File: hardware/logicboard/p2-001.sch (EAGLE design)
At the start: 59 parts, among them IC1 74LS07N, IC11 74LS153D, IC12 LTC485S, IC13 LTC485S, IC2 4066N, J1 MKR, J11 Qwiic, J12 Qwiic, J13 Qwiic, J14 Qwiic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

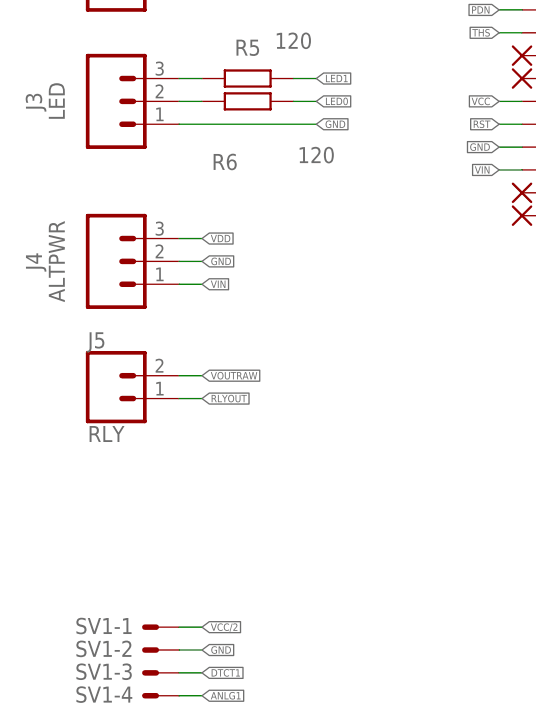
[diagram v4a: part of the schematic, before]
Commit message: Changed Relay port and Alt. Power port.
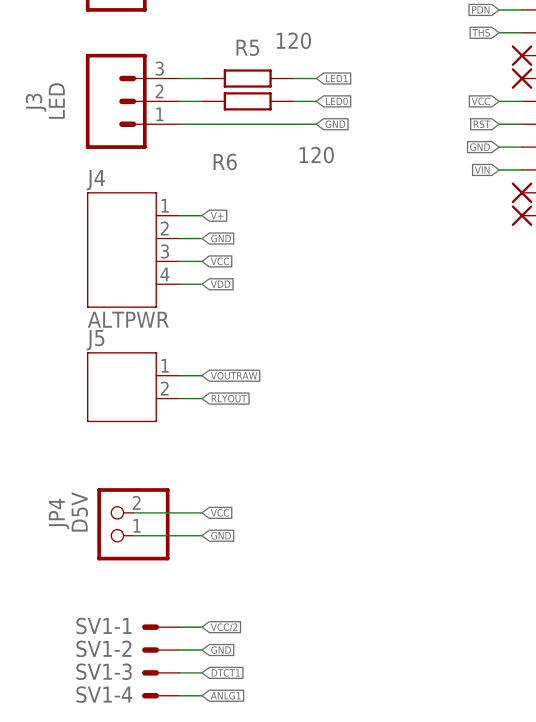
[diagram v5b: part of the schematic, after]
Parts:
- added JP4: D5V, pinhead:PINHD-1X2
- J4: device SparkFun-Connectors:CONN_03JST-PTH-VERT -> jst-ph:JST-PH4
- J5: value RLY -> (none); device SparkFun-Connectors:CONN_02JST-PTH-2 -> jst-ph:JST-PH2
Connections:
- net GND: now also JP4.1
- net RLYOUT: now also J5.2; no longer J5.1
- net V+: now also J4.1
- net VCC: now also J4.3, JP4.2
- net VDD: now also J4.4; no longer J4.3
- net VIN: no longer J4.1
- net VOUTRAW: now also J5.1; no longer J5.2
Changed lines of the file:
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@@
 <part name="SUPPLY54" library="supply2" deviceset="GND" device=""/>
 <part name="JP1" library="pinhead" library_urn="urn:adsk.eagle:library:325" deviceset="PINHD-1X2" device="" package3d_urn="urn:adsk.eagle:package:22435/2" value="MPXJMP"/>
-<part name="J4" library="SparkFun-Connectors" deviceset="CONN_03" device="JST-PTH-VERT" value="ALTPWR"/>
 <part name="D1" library="SparkFun-DiscreteSemi" library_urn="urn:adsk.eagle:library:514" deviceset="DIODE" device="-1N4148" package3d_urn="urn:adsk.eagle:package:38452/1" value=""/>
 <part name="J2" library="SparkFun-Connectors" deviceset="CONN_03" device="JST-PTH-VERT" value="GPIO"/>
@@
 <part name="SUPPLY5" library="supply2" library_urn="urn:adsk.eagle:library:372" deviceset="VCC" device=""/>
 <part name="X14" library="wirepad" library_urn="urn:adsk.eagle:library:412" deviceset="PAD-N" device=""/>
-<part name="J5" library="SparkFun-Connectors" library_urn="urn:adsk.eagle:library:513" deviceset="CONN_02" device="JST-PTH-2" package3d_urn="urn:adsk.eagle:package:38053/1" value="RLY"/>
 <part name="JP3" library="pinhead" library_urn="urn:adsk.eagle:library:325" deviceset="PINHD-2X3" device="" package3d_urn="urn:adsk.eagle:package:22462/2" value="PWRSEL"/>
+<part name="J5" library="jst-ph" deviceset="JST-PH2" device=""/>
+<part name="JP4" library="pinhead" library_urn="urn:adsk.eagle:library:325" deviceset="PINHD-1X2" device="" package3d_urn="urn:adsk.eagle:package:22435/2" value="D5V"/>
+<part name="J4" library="jst-ph" deviceset="JST-PH4" device="" value="ALTPWR"/>
 </parts>
 <sheets>
@@
 <attribute name="VALUE" x="254" y="243.84" size="1.778" layer="96" align="bottom-center"/>
 </instance>
-<instance part="J4" gate="J$1" x="17.78" y="195.58" smashed="yes">
-<attribute name="VALUE" x="12.7" y="195.58" size="1.778" layer="96" rot="R90" align="bottom-center"/>
-<attribute name="NAME" x="10.16" y="195.58" size="1.778" layer="95" rot="R90" align="bottom-center"/>
-</instance>
 <instance part="D1" gate="G$1" x="106.68" y="109.22" smashed="yes" rot="R180">
 <attribute name="NAME" x="106.68" y="114.3" size="1.778" layer="95" align="bottom-center"/>
@@
 </instance>
 <instance part="X14" gate="G$1" x="25.4" y="91.44" smashed="yes"/>
-<instance part="J5" gate="G$1" x="17.78" y="180.34" smashed="yes">
-<attribute name="VALUE" x="15.24" y="175.514" size="1.778" layer="96" font="vector"/>
-<attribute name="NAME" x="15.24" y="185.928" size="1.778" layer="95" font="vector"/>
-</instance>
 <instance part="JP3" gate="A" x="124.46" y="157.48" smashed="yes" rot="R90">
 <attribute name="NAME" x="118.745" y="151.13" size="1.778" layer="95" rot="R90"/>
 <attribute name="VALUE" x="132.08" y="151.13" size="1.778" layer="96" rot="R90"/>
+</instance>
+<instance part="J5" gate="G$1" x="17.78" y="182.88" smashed="yes">
+<attribute name="NAME" x="15.24" y="186.182" size="1.778" layer="95"/>
+<attribute name="VALUE" x="15.24" y="175.514" size="1.778" layer="96"/>
+</instance>
+<instance part="JP4" gate="G$1" x="17.78" y="167.64" smashed="yes" rot="R180">
+<attribute name="NAME" x="12.7" y="167.64" size="1.778" layer="95" rot="R90" align="bottom-center"/>
+<attribute name="VALUE" x="15.24" y="167.64" size="1.778" layer="96" rot="R90" align="bottom-center"/>
+</instance>
+<instance part="J4" gate="A" x="17.78" y="198.12" smashed="yes">
+<attribute name="NAME" x="15.24" y="203.962" size="1.778" layer="95"/>
+<attribute name="VALUE" x="15.24" y="188.214" size="1.778" layer="96"/>
 </instance>
 </instances>
@@
 </segment>
 <segment>
-<pinref part="J4" gate="J$1" pin="2"/>
-<wire x1="25.4" y1="195.58" x2="27.94" y2="195.58" width="0.1524" layer="91"/>
-<label x="27.94" y="195.58" size="0.8128" layer="95" xref="yes"/>
+<pinref part="JP4" gate="G$1" pin="1"/>
+<wire x1="20.32" y1="165.1" x2="27.94" y2="165.1" width="0.1524" layer="91"/>
+<label x="27.94" y="165.1" size="0.8128" layer="95" xref="yes"/>
+</segment>
+<segment>
+<pinref part="J4" gate="A" pin="2"/>
+<wire x1="25.4" y1="198.12" x2="27.94" y2="198.12" width="0.1524" layer="91"/>
+<label x="27.94" y="198.12" size="0.8128" layer="95" xref="yes"/>
 </segment>
 </net>
@@
 <wire x1="124.46" y1="154.94" x2="124.46" y2="147.32" width="0.1524" layer="91"/>
 <label x="124.46" y="147.32" size="0.8128" layer="95" rot="R270" xref="yes"/>
+</segment>
+<segment>
+<pinref part="JP4" gate="G$1" pin="2"/>
+<wire x1="20.32" y1="167.64" x2="27.94" y2="167.64" width="0.1524" layer="91"/>
+<label x="27.94" y="167.64" size="0.8128" layer="95" xref="yes"/>
+</segment>
+<segment>
+<pinref part="J4" gate="A" pin="3"/>
+<wire x1="25.4" y1="195.58" x2="27.94" y2="195.58" width="0.1524" layer="91"/>
+<label x="27.94" y="195.58" size="0.8128" layer="95" xref="yes"/>
 </segment>
 </net>
@@
 </segment>
 <segment>
-<pinref part="J4" gate="J$1" pin="3"/>
-<wire x1="25.4" y1="198.12" x2="27.94" y2="198.12" width="0.1524" layer="91"/>
-<label x="27.94" y="198.12" size="0.8128" layer="95" xref="yes"/>
+<pinref part="J4" gate="A" pin="4"/>
+<wire x1="25.4" y1="193.04" x2="27.94" y2="193.04" width="0.1524" layer="91"/>
+<label x="27.94" y="193.04" size="0.8128" layer="95" xref="yes"/>
 </segment>
 </net>
@@
 </net>
 <net name="VIN" class="2">
-<segment>
-<pinref part="J4" gate="J$1" pin="1"/>
-<wire x1="25.4" y1="193.04" x2="27.94" y2="193.04" width="0.1524" layer="91"/>
-<label x="27.94" y="193.04" size="0.8128" layer="95" xref="yes"/>
-</segment>
 <segment>
 <pinref part="MC1" gate="G$1" pin="9V"/>
@@
 </segment>
 <segment>
-<pinref part="J5" gate="G$1" pin="2"/>
 <wire x1="25.4" y1="182.88" x2="27.94" y2="182.88" width="0.1524" layer="91"/>
 <label x="27.94" y="182.88" size="0.8128" layer="95" xref="yes"/>
+<pinref part="J5" gate="G$1" pin="1"/>
 </segment>
 </net>
@@
 </segment>
 <segment>
-<pinref part="J5" gate="G$1" pin="1"/>
 <wire x1="25.4" y1="180.34" x2="27.94" y2="180.34" width="0.1524" layer="91"/>
 <label x="27.94" y="180.34" size="0.8128" layer="95" xref="yes"/>
+<pinref part="J5" gate="G$1" pin="2"/>
 </segment>
 </net>
@@
 <label x="121.92" y="147.32" size="0.8128" layer="95" rot="R270" xref="yes"/>
 </segment>
-</net>
+<segment>
+<pinref part="J4" gate="A" pin="1"/>
+<wire x1="25.4" y1="200.66" x2="27.94" y2="200.66" width="0.1524" layer="91"/>
+<label x="27.94" y="200.66" size="0.8128" layer="95" xref="yes"/>
+</segment>
+</net>

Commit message: List of components.
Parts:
- removed R6: 120, resistor:R-EU_0204/5
- added R4: 120, resistor:R-EU_0204/5
- renumbered J6 to JP5
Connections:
- net LED0: now also R5.2; no longer R6.2
- net LED0A: now also R5.1; no longer R6.1
- net LED1: now also R4.2; no longer R5.2
- net LED1A: now also R4.1; no longer R5.1
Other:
- moved on the sheet: R5
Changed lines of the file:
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@@
 <part name="SUPPLY29" library="supply2" deviceset="GND" device=""/>
 <part name="J1" library="SparkFun-Connectors" library_urn="urn:adsk.eagle:library:513" deviceset="CONN_05" device="JST" package3d_urn="urn:adsk.eagle:package:38120/1" value="MKR"/>
-<part name="R5" library="resistor" library_urn="urn:adsk.eagle:library:348" deviceset="R-EU_" device="0204/5" package3d_urn="urn:adsk.eagle:package:23488/1" value="120"/>
+<part name="R4" library="resistor" library_urn="urn:adsk.eagle:library:348" deviceset="R-EU_" device="0204/5" package3d_urn="urn:adsk.eagle:package:23488/1" value="120"/>
 <part name="SUPPLY12" library="supply2" deviceset="GND" device=""/>
 <part name="JP0" library="pinhead" library_urn="urn:adsk.eagle:library:325" deviceset="PINHD-1X1" device="" package3d_urn="urn:adsk.eagle:package:22485/2" value="GNDPIN"/>
@@
 <part name="H1" library="SparkFun-Hardware" library_urn="urn:adsk.eagle:library:519" deviceset="STAND-OFF" device="" package3d_urn="urn:adsk.eagle:package:38630/1"/>
 <part name="H2" library="SparkFun-Hardware" library_urn="urn:adsk.eagle:library:519" deviceset="STAND-OFF" device="" package3d_urn="urn:adsk.eagle:package:38630/1"/>
-<part name="J6" library="SparkFun-Connectors" library_urn="urn:adsk.eagle:library:513" deviceset="CONN_05" device="" package3d_urn="urn:adsk.eagle:package:38104/1" value="RTC"/>
+<part name="JP5" library="SparkFun-Connectors" library_urn="urn:adsk.eagle:library:513" deviceset="CONN_05" device="" package3d_urn="urn:adsk.eagle:package:38104/1" value="RTC"/>
 <part name="J3" library="SparkFun-Connectors" deviceset="CONN_03" device="JST-PTH" value="LED"/>
-<part name="R6" library="resistor" library_urn="urn:adsk.eagle:library:348" deviceset="R-EU_" device="0204/5" package3d_urn="urn:adsk.eagle:package:23488/1" value="120"/>
+<part name="R5" library="resistor" library_urn="urn:adsk.eagle:library:348" deviceset="R-EU_" device="0204/5" package3d_urn="urn:adsk.eagle:package:23488/1" value="120"/>
 <part name="X6" library="wirepad" library_urn="urn:adsk.eagle:library:412" deviceset="PAD-N" device=""/>
 <part name="IC11" library="74xx-us" library_urn="urn:adsk.eagle:library:88" deviceset="74*153" device="D" package3d_urn="urn:adsk.eagle:package:2918/1" technology="LS"/>
@@
 <attribute name="NAME" x="10.16" y="246.38" size="1.778" layer="95" rot="R90" align="bottom-center"/>
 </instance>
-<instance part="R5" gate="G$1" x="33.02" y="215.9" smashed="yes">
+<instance part="R4" gate="G$1" x="33.02" y="215.9" smashed="yes">
 <attribute name="NAME" x="33.02" y="218.44" size="1.778" layer="95" align="bottom-center"/>
 <attribute name="VALUE" x="38.1" y="220.98" size="1.778" layer="96" align="top-center"/>
@@
 <instance part="H1" gate="G$1" x="12.7" y="86.36" smashed="yes"/>
 <instance part="H2" gate="G$1" x="12.7" y="96.52" smashed="yes"/>
-<instance part="J6" gate="G$1" x="17.78" y="91.44" smashed="yes">
+<instance part="JP5" gate="G$1" x="17.78" y="91.44" smashed="yes">
 <attribute name="VALUE" x="12.7" y="91.44" size="1.778" layer="96" rot="R90" align="bottom-center"/>
 <attribute name="NAME" x="10.16" y="91.44" size="1.778" layer="95" font="vector" rot="R90" align="bottom-center"/>
@@
 <attribute name="NAME" x="10.16" y="213.36" size="1.778" layer="95" rot="R90" align="bottom-center"/>
 </instance>
-<instance part="R6" gate="G$1" x="33.02" y="213.36" smashed="yes">
-<attribute name="NAME" x="30.48" y="205.74" size="1.778" layer="95" align="bottom-center"/>
+<instance part="R5" gate="G$1" x="33.02" y="213.36" smashed="yes">
+<attribute name="NAME" x="33.02" y="208.28" size="1.778" layer="95" align="bottom-center"/>
 <attribute name="VALUE" x="40.64" y="208.28" size="1.778" layer="96" align="top-center"/>
 </instance>
@@
 </segment>
 <segment>
-<pinref part="J6" gate="G$1" pin="2"/>
+<pinref part="JP5" gate="G$1" pin="2"/>
 <wire x1="25.4" y1="88.9" x2="27.94" y2="88.9" width="0.1524" layer="91"/>
 <label x="27.94" y="88.9" size="0.8128" layer="95" xref="yes"/>
@@
 </segment>
 <segment>
-<pinref part="J6" gate="G$1" pin="1"/>
+<pinref part="JP5" gate="G$1" pin="1"/>
 <wire x1="25.4" y1="86.36" x2="27.94" y2="86.36" width="0.1524" layer="91"/>
 <label x="27.94" y="86.36" size="0.8128" layer="95" xref="yes"/>
@@
 </segment>
 <segment>
-<pinref part="J6" gate="G$1" pin="5"/>
+<pinref part="JP5" gate="G$1" pin="5"/>
 <wire x1="25.4" y1="96.52" x2="27.94" y2="96.52" width="0.1524" layer="91"/>
 <label x="27.94" y="96.52" size="0.8128" layer="95" xref="yes"/>
@@
 </segment>
 <segment>
-<pinref part="J6" gate="G$1" pin="4"/>
+<pinref part="JP5" gate="G$1" pin="4"/>
 <wire x1="25.4" y1="93.98" x2="27.94" y2="93.98" width="0.1524" layer="91"/>
 <label x="27.94" y="93.98" size="0.8128" layer="95" xref="yes"/>
@@
 </segment>
 <segment>
-<pinref part="R6" gate="G$1" pin="2"/>
+<pinref part="R5" gate="G$1" pin="2"/>
 <wire x1="38.1" y1="213.36" x2="40.64" y2="213.36" width="0.1524" layer="91"/>
 <label x="40.64" y="213.36" size="0.8128" layer="95" xref="yes"/>
@@
 </segment>
 <segment>
-<pinref part="R5" gate="G$1" pin="2"/>
+<pinref part="R4" gate="G$1" pin="2"/>
 <wire x1="38.1" y1="215.9" x2="40.64" y2="215.9" width="0.1524" layer="91"/>
 <label x="40.64" y="215.9" size="0.8128" layer="95" xref="yes"/>
@@
 <net name="LED0A" class="0">
 <segment>
-<pinref part="R6" gate="G$1" pin="1"/>
+<pinref part="R5" gate="G$1" pin="1"/>
 <pinref part="J3" gate="J$1" pin="2"/>
 <wire x1="27.94" y1="213.36" x2="25.4" y2="213.36" width="0.1524" layer="91"/>
@@
 <net name="LED1A" class="0">
 <segment>
-<pinref part="R5" gate="G$1" pin="1"/>
+<pinref part="R4" gate="G$1" pin="1"/>
 <pinref part="J3" gate="J$1" pin="3"/>
 <wire x1="27.94" y1="215.9" x2="25.4" y2="215.9" width="0.1524" layer="91"/>

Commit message: Added pads to connect MIDI IN and RX.
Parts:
- added IN, RX: (no value), wirepad:SMD2
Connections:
- net MIN: now also IN.P
- net RX: now also RX.P
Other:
- note added: "226 = 22u 105 = 1u 474 = 470n 104 = 100n 103 = 10n"
- moved on the sheet: D3, IC11, IC12, IC13, IC1A, IC1B, IC1C, JP1, OK1, R11, R12, R13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

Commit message: Renumbered connectors. Fixed error of silk pattern.
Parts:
- J3: value LED -> ALTPWR; device SparkFun-Connectors:CONN_03JST-PTH -> jst-ph:JST-PH4
- J4: value ALTPWR -> (none); device jst-ph:JST-PH4 -> jst-ph:JST-PH2
- J5: value (none) -> LED; device jst-ph:JST-PH2 -> SparkFun-Connectors:CONN_03JST-PTH
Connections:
- net GND: now also J3.2, J5.1; no longer J3.1, J4.2
- net LED0A: now also J5.2; no longer J3.2
- net LED1A: now also J5.3; no longer J3.3
- net RLYOUT: now also J4.2; no longer J5.2
- net V+: now also J3.1; no longer J4.1
- net VCC: now also J3.3; no longer J4.3
- net VDD: now also J3.4; no longer J4.4
- net VOUTRAW: now also J4.1; no longer J5.1
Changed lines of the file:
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@@
 <part name="H2" library="SparkFun-Hardware" library_urn="urn:adsk.eagle:library:519" deviceset="STAND-OFF" device="" package3d_urn="urn:adsk.eagle:package:38630/1"/>
 <part name="JP5" library="SparkFun-Connectors" library_urn="urn:adsk.eagle:library:513" deviceset="CONN_05" device="" package3d_urn="urn:adsk.eagle:package:38104/1" value="RTC"/>
-<part name="J3" library="SparkFun-Connectors" deviceset="CONN_03" device="JST-PTH" value="LED"/>
+<part name="J5" library="SparkFun-Connectors" deviceset="CONN_03" device="JST-PTH" value="LED"/>
 <part name="R5" library="resistor" library_urn="urn:adsk.eagle:library:348" deviceset="R-EU_" device="0204/5" package3d_urn="urn:adsk.eagle:package:23488/1" value="120"/>
 <part name="X6" library="wirepad" library_urn="urn:adsk.eagle:library:412" deviceset="PAD-N" device=""/>
@@
 <part name="X14" library="wirepad" library_urn="urn:adsk.eagle:library:412" deviceset="PAD-N" device=""/>
 <part name="JP3" library="pinhead" library_urn="urn:adsk.eagle:library:325" deviceset="PINHD-2X3" device="" package3d_urn="urn:adsk.eagle:package:22462/2" value="PWRSEL"/>
-<part name="J5" library="jst-ph" deviceset="JST-PH2" device=""/>
+<part name="J4" library="jst-ph" deviceset="JST-PH2" device=""/>
 <part name="JP4" library="pinhead" library_urn="urn:adsk.eagle:library:325" deviceset="PINHD-1X2" device="" package3d_urn="urn:adsk.eagle:package:22435/2" value="D5V"/>
-<part name="J4" library="jst-ph" deviceset="JST-PH4" device="" value="ALTPWR"/>
+<part name="J3" library="jst-ph" deviceset="JST-PH4" device="" value="ALTPWR"/>
 <part name="RX" library="wirepad" library_urn="urn:adsk.eagle:library:412" deviceset="SMD2" device="" package3d_urn="urn:adsk.eagle:package:30839/1"/>
 <part name="IN" library="wirepad" library_urn="urn:adsk.eagle:library:412" deviceset="SMD2" device="" package3d_urn="urn:adsk.eagle:package:30839/1"/>
@@
 <attribute name="NAME" x="10.16" y="91.44" size="1.778" layer="95" font="vector" rot="R90" align="bottom-center"/>
 </instance>
-<instance part="J3" gate="J$1" x="17.78" y="213.36" smashed="yes">
+<instance part="J5" gate="J$1" x="17.78" y="213.36" smashed="yes">
 <attribute name="VALUE" x="12.7" y="213.36" size="1.778" layer="96" rot="R90" align="bottom-center"/>
 <attribute name="NAME" x="10.16" y="213.36" size="1.778" layer="95" rot="R90" align="bottom-center"/>
@@
 <attribute name="VALUE" x="132.08" y="151.13" size="1.778" layer="96" rot="R90"/>
 </instance>
-<instance part="J5" gate="G$1" x="17.78" y="182.88" smashed="yes">
+<instance part="J4" gate="G$1" x="17.78" y="182.88" smashed="yes">
 <attribute name="NAME" x="15.24" y="186.182" size="1.778" layer="95"/>
 <attribute name="VALUE" x="15.24" y="175.514" size="1.778" layer="96"/>
@@
 <attribute name="VALUE" x="15.24" y="167.64" size="1.778" layer="96" rot="R90" align="bottom-center"/>
 </instance>
-<instance part="J4" gate="A" x="17.78" y="198.12" smashed="yes">
+<instance part="J3" gate="A" x="17.78" y="198.12" smashed="yes">
 <attribute name="NAME" x="15.24" y="203.962" size="1.778" layer="95"/>
 <attribute name="VALUE" x="15.24" y="188.214" size="1.778" layer="96"/>
@@
 </segment>
 <segment>
-<pinref part="J3" gate="J$1" pin="1"/>
+<pinref part="J5" gate="J$1" pin="1"/>
 <wire x1="25.4" y1="210.82" x2="40.64" y2="210.82" width="0.1524" layer="91"/>
 <label x="40.64" y="210.82" size="0.8128" layer="95" xref="yes"/>
@@
 </segment>
 <segment>
-<pinref part="J4" gate="A" pin="2"/>
+<pinref part="J3" gate="A" pin="2"/>
 <wire x1="25.4" y1="198.12" x2="27.94" y2="198.12" width="0.1524" layer="91"/>
 <label x="27.94" y="198.12" size="0.8128" layer="95" xref="yes"/>
@@
 </segment>
 <segment>
-<pinref part="J4" gate="A" pin="3"/>
+<pinref part="J3" gate="A" pin="3"/>
 <wire x1="25.4" y1="195.58" x2="27.94" y2="195.58" width="0.1524" layer="91"/>
 <label x="27.94" y="195.58" size="0.8128" layer="95" xref="yes"/>
@@
 </segment>
 <segment>
-<pinref part="J4" gate="A" pin="4"/>
+<pinref part="J3" gate="A" pin="4"/>
 <wire x1="25.4" y1="193.04" x2="27.94" y2="193.04" width="0.1524" layer="91"/>
 <label x="27.94" y="193.04" size="0.8128" layer="95" xref="yes"/>
@@
 <segment>
 <pinref part="R5" gate="G$1" pin="1"/>
-<pinref part="J3" gate="J$1" pin="2"/>
+<pinref part="J5" gate="J$1" pin="2"/>
 <wire x1="27.94" y1="213.36" x2="25.4" y2="213.36" width="0.1524" layer="91"/>
 </segment>
@@
 <segment>
 <pinref part="R4" gate="G$1" pin="1"/>
-<pinref part="J3" gate="J$1" pin="3"/>
+<pinref part="J5" gate="J$1" pin="3"/>
 <wire x1="27.94" y1="215.9" x2="25.4" y2="215.9" width="0.1524" layer="91"/>
 </segment>
@@
 <wire x1="25.4" y1="182.88" x2="27.94" y2="182.88" width="0.1524" layer="91"/>
 <label x="27.94" y="182.88" size="0.8128" layer="95" xref="yes"/>
-<pinref part="J5" gate="G$1" pin="1"/>
+<pinref part="J4" gate="G$1" pin="1"/>
 </segment>
 </net>
@@
 <wire x1="25.4" y1="180.34" x2="27.94" y2="180.34" width="0.1524" layer="91"/>
 <label x="27.94" y="180.34" size="0.8128" layer="95" xref="yes"/>
-<pinref part="J5" gate="G$1" pin="2"/>
+<pinref part="J4" gate="G$1" pin="2"/>
 </segment>
 </net>
@@
 </segment>
 <segment>
-<pinref part="J4" gate="A" pin="1"/>
+<pinref part="J3" gate="A" pin="1"/>
 <wire x1="25.4" y1="200.66" x2="27.94" y2="200.66" width="0.1524" layer="91"/>
 <label x="27.94" y="200.66" size="0.8128" layer="95" xref="yes"/>
